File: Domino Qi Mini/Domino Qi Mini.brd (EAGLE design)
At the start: 55.9 x 33 mm, 97 parts, among them J1 MH22-1, J2 MH22-1, M1 DOMINO, Q1 AP2302GN, Q2 2SC4081, SW1 IT-1100, SW2 IT-1100, SW3 IT-1100, U1 ATMEGA32U4-XUMU, U2 MP2162GQH, U3 NTB0104GU12, U4 NTB0102GU, U5 MAX3375EEKA+T, Y1 16MHz

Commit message: Domino Qi Mini: work in progress
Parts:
- removed U$39: (no value), Domino:RECYCLE_BIN_LOGO
- removed U$41: (no value), Domino:CE_LOGO_SMALL
- removed U$9: (no value), Domino:DOMINO_LOGO_SMALL
- added U$3, U$5: (no value), Domino:DOMINO_QI_LOGO_SMALL
- S1: value USB_MR5-003A -> USB_MR5-001; device Domino:USB_MR5-003A -> Domino:USB-MR5-001
- SW1, SW2, SW3: value IT-1100 -> IT-1210; device Domino:IT-1100 -> Domino:IT-1210
- U$7: value (none) -> DOMINO_QI_LOGO; device Domino:DOMINO_LOGO_SMALL -> Domino:DOMINO_QI_LOGO
- U1: value ATMEGA32U4-XUMU -> ATMEGA32U4-XUAU/MU; device Domino:QFN44ML7X7 -> Domino:ATMEGA32U4_DUAL_FOOTPRINT
- moved U$7 98.7 mm to (-34.3, -47.0)
- moved SW2 60.9 mm to (0.64, 6.48), flipped to the bottom, turned to 270 degrees
- moved SW3 56.7 mm to (54.9, 26.9)
- moved SW1 46.3 mm to (0.64, 26.4), flipped to the bottom, turned to 270 degrees
- moved R23 45.2 mm to (51.8, 24.8), turned to 270 degrees
- moved C29 43.8 mm to (50.8, 24.8), turned to 90 degrees
- moved D9 37.9 mm to (41.6, 4.39), flipped to the bottom
- moved C14 34.2 mm to (31.9, 7.49), flipped to the bottom, turned to 270 degrees
- moved U1 34.1 mm to (27.9, 15.2), flipped to the bottom, turned to 180 degrees
- moved D8 33.8 mm to (22.5, 28.5), flipped to the bottom
- moved R8 33.5 mm to (20.4, 6.48), flipped to the bottom
- moved U4 32.2 mm to (22.7, 7.24), flipped to the bottom
- moved R17 31.6 mm to (25.0, 5.97), flipped to the bottom
- moved Q1 30.8 mm to (11.4, 27.9), flipped to the bottom
- moved C27 30.7 mm to (24.5, 7.49), flipped to the bottom, turned to 90 degrees
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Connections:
- net !RESET: now also SW1.1, U1.13A, U1.13M; no longer SW1.2, U1.13
- net +5V: now also U1.14A, U1.14M, U1.24A, U1.24M, U1.2A, U1.2M, U1.34A, U1.34M, U1.44A, U1.44M, U1.7A, U1.7M; no longer U1.14, U1.2, U1.24, U1.34, U1.44, U1.7
- net A0: now also U1.36A, U1.36M; no longer U1.36
- net A1: now also U1.37A, U1.37M; no longer U1.37
- net A2: now also U1.38A, U1.38M; no longer U1.38
- net A3: now also U1.39A, U1.39M; no longer U1.39
- net A4: now also U1.40A, U1.40M; no longer U1.40
- net A5: now also U1.41A, U1.41M; no longer U1.41
- net AREF: now also U1.42A, U1.42M; no longer U1.42
- net D+: now also D1.2; no longer D1.3
- net D-: now also D1.3; no longer D1.2
- net D4: now also U1.25A, U1.25M; no longer U1.25
- net D5: now also U1.31A, U1.31M; no longer U1.31
- net D6: now also U1.27A, U1.27M; no longer U1.27
- net GND: now also SW1.2, SW1.SH$1, SW1.SH$2, SW2.SH$1, SW2.SH$2, SW3.SH$1, SW3.SH$2, U1.15A, U1.15M, U1.23A, U1.23M, U1.35A, U1.35M, U1.43A, U1.43M, U1.5A, U1.5M, U1.PAD; no longer SW1.1, SW1.S$1, SW1.S$2, SW2.S$1, SW2.S$2, SW3.S$1, SW3.S$2, U1.15, U1.23, U1.35, U1.43, U1.5, U1.EXP
- net HANDSHAKE: now also U1.1A, U1.1M; no longer U1.1
- net IO10: now also U1.30A, U1.30M; no longer U1.30
- net IO11: now also U1.12A, U1.12M; no longer U1.12
- net IO12: now also U1.26M
- net IO13: now also U1.32A, U1.32M; no longer U1.32
- net IO8: now also U1.28A, U1.28M; no longer U1.28
- net IO9: now also U1.29A, U1.29M; no longer U1.29
- net MISO: now also U1.11A, U1.11M; no longer U1.11
- net MOSI: now also U1.10A, U1.10M; no longer U1.10
- net N$5: now also U1.3A, U1.3M; no longer U1.3
- net N$8: now also U1.33A, U1.33M; no longer U1.33
- net N$9: now also U1.4A, U1.4M; no longer U1.4
- net PE: now also S1.SH$1, S1.SH$2, S1.SH$3, S1.SH$4; no longer S1.S$1, S1.S$2, S1.S$3
- net RXD1: now also U1.20A, U1.20M; no longer U1.20
- net SCK: now also U1.9A, U1.9M; no longer U1.9
- net SCL: now also U1.18A, U1.18M; no longer U1.18
- net SDA: now also U1.19A, U1.19M; no longer U1.19
- net SS: now also U1.8A, U1.8M; no longer U1.8
- net TXD1: now also U1.21A, U1.21M; no longer U1.21
- net UCAP: now also U1.6A, U1.6M; no longer U1.6
- net XTAL1: now also U1.17A, U1.17M; no longer U1.17
- net XTAL2: now also U1.16A, U1.16M; no longer U1.16
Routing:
- net UART_RTS: track 75.6 -> 0.00 mm, vias 3 -> 0
- net GP6: track 0.00 -> 53.6 mm, vias 0 -> 3
- net AREF: track 0.00 -> 51.0 mm, vias 0 -> 3
- net +5V: track 46.5 -> 96.3 mm, vias 1 -> 2
- net I2S_MCK: track 7.10 -> 47.1 mm, vias 1 -> 3
- net MISO: track 0.00 -> 38.5 mm, vias 0 -> 1
- net SPDIF_OUT: track 8.13 -> 46.5 mm
- net !RESET: track 0.00 -> 37.7 mm
- net SS: track 0.00 -> 36.6 mm, vias 0 -> 1
- net A0: track 0.00 -> 36.4 mm, vias 0 -> 1
- net D6: track 0.00 -> 35.5 mm, vias 0 -> 1
- net MOSI: track 0.00 -> 35.2 mm, vias 0 -> 1
- net SCK: track 0.00 -> 34.8 mm, vias 0 -> 1
- net A1: track 0.00 -> 34.0 mm, vias 0 -> 1
- net D5: track 0.00 -> 33.6 mm, vias 0 -> 1
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- removed copper zone on layer 16, net +2V5
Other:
- board text removed: "CTS"
- board text removed: "Domino Core"
- board text removed: "Domino Pi"
- board text removed: "Domino Qi"
- board text removed: "MCK"
- board text removed: "MICIN"
- board text removed: "RTS"
- board text removed: "RX"
- board text removed: "SD"
- board text removed: "TX"
- board text removed: "WS"

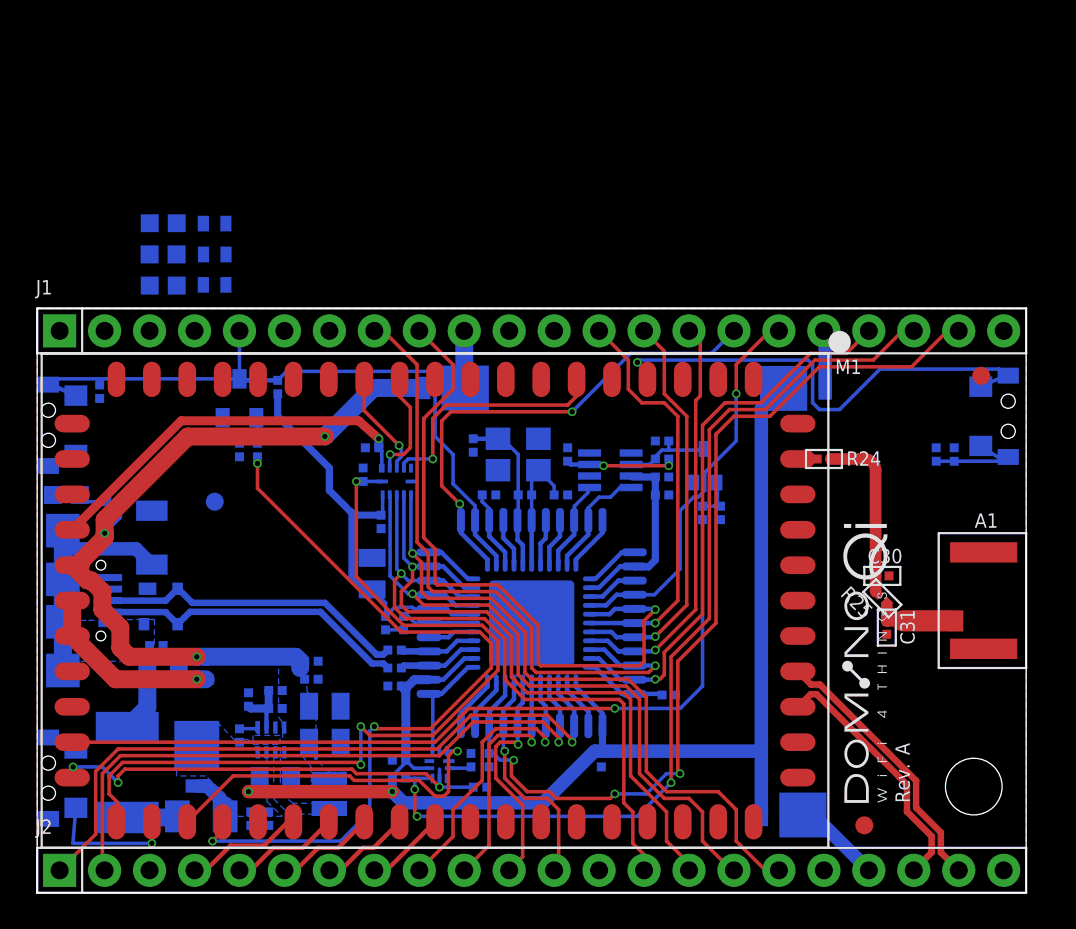
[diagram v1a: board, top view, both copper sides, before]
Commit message: Work in progress: changed for PCB antenna and removed Schottky diode on Domino Qi Mini, first Domino Qi draft
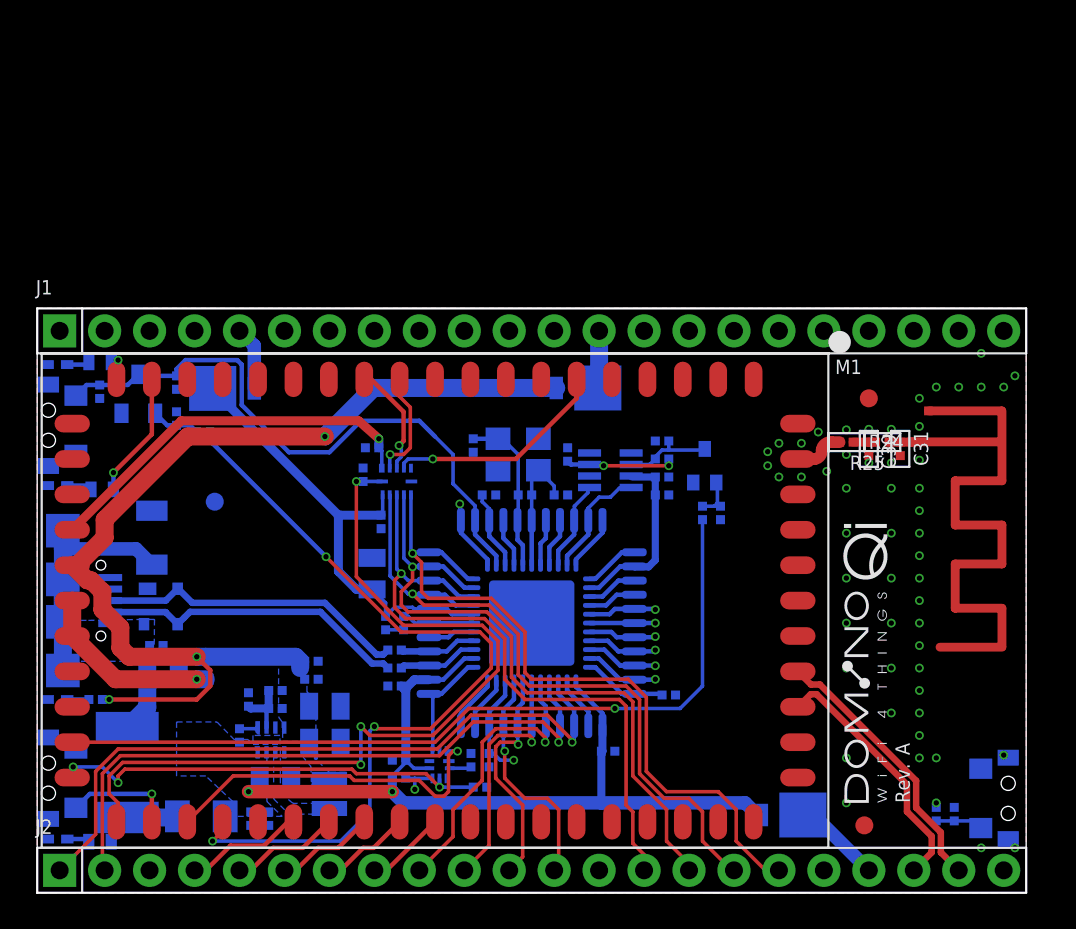
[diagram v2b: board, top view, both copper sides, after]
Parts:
- removed D2: MBRM130LT1G, Domino:DO-216AA
- A1: value ACA-5036-A2-CC-S -> RF_ANT1; device Domino:ACA-5036-A2-CC-S -> Domino:RF_ANT1
- D3, D4, D5, D6: device Domino:LED0603 -> Domino:LED0402
- moved R20 35.5 mm to (3.55, 2.89), turned to 180 degrees
- moved D4 35.3 mm to (1.15, 3.04)
- moved D7 32.3 mm to (11.6, 28.5)
- moved SW3 21.6 mm to (54.9, 5.33)
- moved C29 20.3 mm to (50.8, 4.45)
- moved R23 20.3 mm to (51.8, 4.45)
- moved R21 13.2 mm to (3.67, 22.8), turned to 180 degrees
- moved D5 12.8 mm to (1.15, 23.0)
- moved D3 11.6 mm to (1.14, 10.9)
- moved A1 11.3 mm to (49.9, 27.2)
- moved R18 11.2 mm to (3.30, 10.9)
- moved C31 10.1 mm to (48.8, 25.1)
- moved R22 8.89 mm to (3.56, 30.0)
- moved R25 8.83 mm to (47.8, 25.5), turned to 0 degrees
- moved D6 8.62 mm to (1.14, 29.8)
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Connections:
- removed net +VUSB: D2.2, L1.1
- net !RESET: now also J1.18; no longer J1.5
- net +5V: now also L1.1; no longer D2.1
- net 3V3: now also J1.13; no longer J1.10
- net AREF: now also J1.2; no longer J1.21
- net D4: now also J1.16; no longer J1.7
- net D5: now also J1.15; no longer J1.8
- net D6: now also J1.14; no longer J1.9
- net GND: now also A1.GND, J1.12; no longer A1.GND$1, A1.GND$2, J1.11
- net GP6: now also J1.3; no longer J1.20
- net HANDSHAKE: now also J1.11; no longer J1.12
- net IO10: now also J1.8; no longer J1.15
- net IO11: now also J1.7; no longer J1.16
- net IO12: now also J1.6; no longer J1.17
- net IO13: now also J1.4; no longer J1.19
- net IO8: now also J1.10; no longer J1.13
- net IO9: now also J1.9; no longer J1.14
- net RXD1: now also J1.21; no longer J1.2
- net SCL: now also J1.17; no longer J1.6
- net SDA: now also J1.19; no longer J1.4
- net TXD1: now also J1.20; no longer J1.3
- net VIN: now also J1.5; no longer J1.18
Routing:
- net GP6: track 53.6 -> 2.13 mm, vias 3 -> 1
- net AREF: track 51.0 -> 3.13 mm, vias 3 -> 1
- net D6: track 35.5 -> 1.20 mm
- net D5: track 33.6 -> 1.19 mm
- net IO13: track 28.4 -> 1.20 mm
- net !RESET_L: track 27.1 -> 0.39 mm, vias 1 -> 0
- net IO11: track 24.8 -> 1.08 mm, vias 2 -> 1
- net IO8: track 20.8 -> 1.18 mm
- net IO12: track 19.4 -> 0.00 mm, vias 1 -> 0
- net IO10: track 20.6 -> 1.22 mm
- net IO9: track 20.2 -> 1.20 mm
- net +5V: track 96.3 -> 78.4 mm
- net +3V3: track 44.7 -> 58.5 mm
- net ANT0_EXT: track 9.82 -> 1.27 mm
- net LED1: track 0.77 -> 7.88 mm, vias 0 -> 1
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
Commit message: Work in progress on Domino Qi Mini board
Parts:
- removed C2: 10u, Domino:C0805
- removed C3: 100n, Domino:C0402
- removed D7, D8, D9: MBRM130LT1G, Domino:DO-216AA
- removed F1: 0ZCG0110FF2C, Domino:PTC1812
- removed L1: BLM31PG601SN1L, Domino:FB1206
- added C32: 100n, Domino:C0402
- added C33: 4u7, Domino:C0805
- added C34: 10n, Domino:C0402
- added L3: BLM31PG601SN1L, Domino:FB1206
- added R26: 100k, Domino:R0402
- added R27: 15k, Domino:R0402
- added R28: 0R, Domino:R0402
- added U6: MP65151DJ, Domino:SOT23-6
- R1, R2: device GeMiNi:R0402 -> Domino:R0402
- moved U$42 7.05 mm to (15.7, 2.79), turned to 270 degrees
- moved C25 6.13 mm to (9.40, 12.4), turned to 90 degrees
- moved R18 5.99 mm to (9.02, 9.14)
- moved L2 5.47 mm to (16.3, 11.0)
- moved R14 5.22 mm to (5.97, 22.1)
- moved C24 5.09 mm to (10.4, 12.4), turned to 90 degrees
- moved C22 4.67 mm to (11.9, 12.3), turned to 90 degrees
- moved C23 4.44 mm to (14.0, 12.3), turned to 90 degrees
- moved R12 4.15 mm to (5.97, 23.1), turned to 180 degrees
- moved C16 3.07 mm to (11.0, 9.53), turned to 90 degrees
- moved R6 2.95 mm to (11.6, 8.00), turned to 180 degrees
- moved Q1 2.85 mm to (4.70, 25.5)
- moved R5 2.57 mm to (13.6, 7.49), turned to 0 degrees
- moved R9 2.40 mm to (5.84, 27.6)
- moved R8 2.16 mm to (22.0, 4.95), turned to 270 degrees
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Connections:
- removed net 5V: D9.1, J2.19
- removed net VPROT: F1.1, L1.2
- new net !FLAG: R28.1, U6.4
- new net EN_USB: R26.1, R28.2, U6.3
- new net ILIM: R27.1, U6.5
- net +3V3: now also J1.13; no longer D8.2
- net +5V: now also J1.5, J2.19, U6.6; no longer D7.1, D9.2, L1.1
- net 3V3: no longer D8.1, J1.13
- net GND: now also C32.2, C33.2, C34.2, R27.2, U6.2; no longer C2.2, C3.2
- net VBUS: now also C34.1, L3.2; no longer C2.1, C3.1, F1.2
- net VIN: now also C32.1, C33.1, L3.1, R26.2, U6.1; no longer D7.2, J1.5
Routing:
- net !RESET_L: track 0.39 -> 33.4 mm, vias 0 -> 1
- net D5: track 1.19 -> 26.4 mm, vias 1 -> 3
- net UART_RTS: track 0.00 -> 25.0 mm, vias 0 -> 1
- net RXD1: track 2.22 -> 26.8 mm, vias 0 -> 1
- net SDA: track 0.00 -> 22.7 mm, vias 0 -> 1
- net +3V3: track 58.5 -> 37.2 mm, vias 3 -> 4
- net TXD1: track 3.62 -> 24.8 mm, vias 0 -> 1
- net LED6: track 0.00 -> 20.3 mm, vias 0 -> 2
- net SCL: track 0.00 -> 20.0 mm, vias 0 -> 1
- net D4: track 0.00 -> 17.0 mm, vias 0 -> 1
- net !RESET: track 31.7 -> 42.6 mm, vias 0 -> 2
- net POWER_LED: track 1.23 -> 7.59 mm
- net +3.3VD_IN: track 10.9 -> 15.9 mm, vias 1 -> 3
- net 5V: track 5.02 -> 0.00 mm
- net +5V: track 78.4 -> 73.6 mm, vias 2 -> 0
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- added copper zone on layer 16, net VIN
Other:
- board text added: "c 2014-2015, Domino Team All rights reserved."
- board text added: "© 2014-2015, The Domino Team. All rights reserved."
- board text removed: "SLOT SIZE IN MM 2x PLATED SLOT: 0.9x0.4"
- board text removed: "SLOT SIZE IN MM 2x PLATED SLOT: 1.3x0.5"
- board text removed: "c 2014, Domino Team All rights reserved."
- board text removed: "© 2014, The Domino Team. All rights reserved."

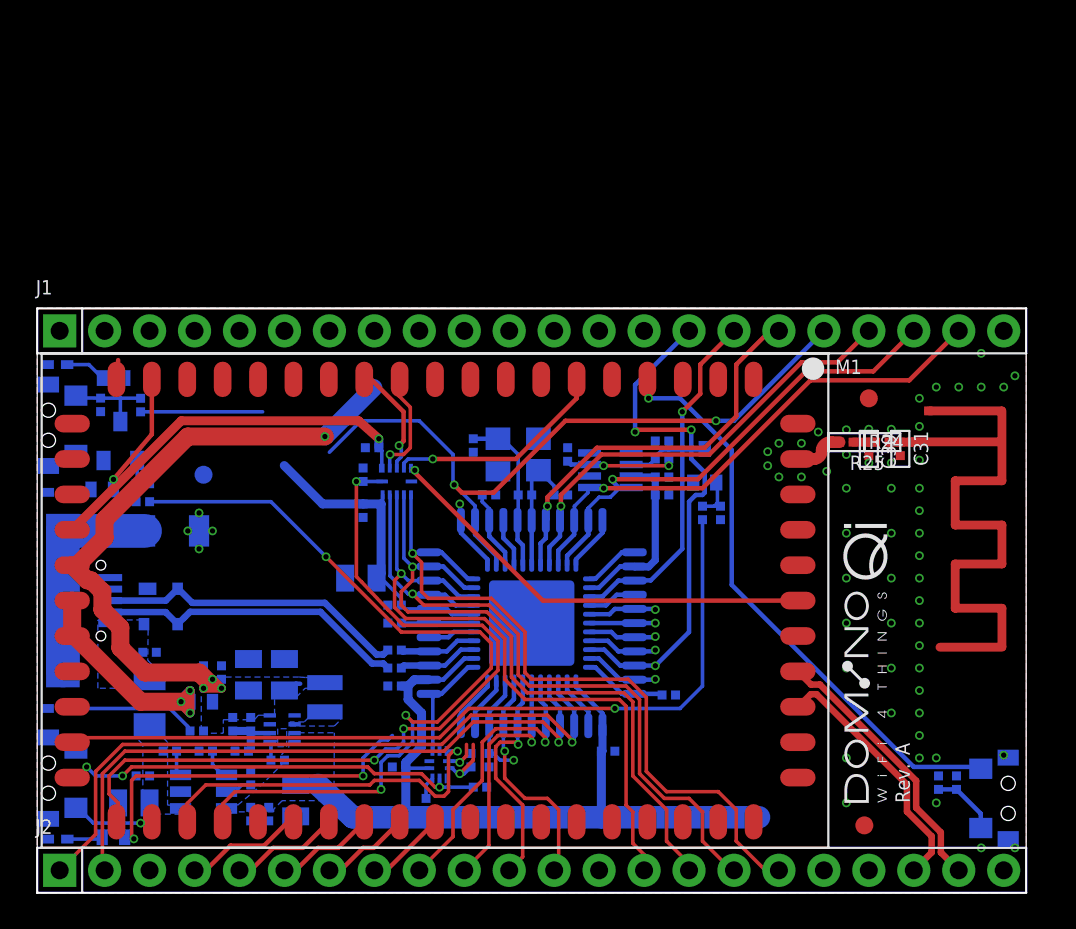
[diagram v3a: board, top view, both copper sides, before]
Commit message: Work in progress on Domino Qi Mini board: clustered all voltage translator chips instead of putting them close to ATMega32U4
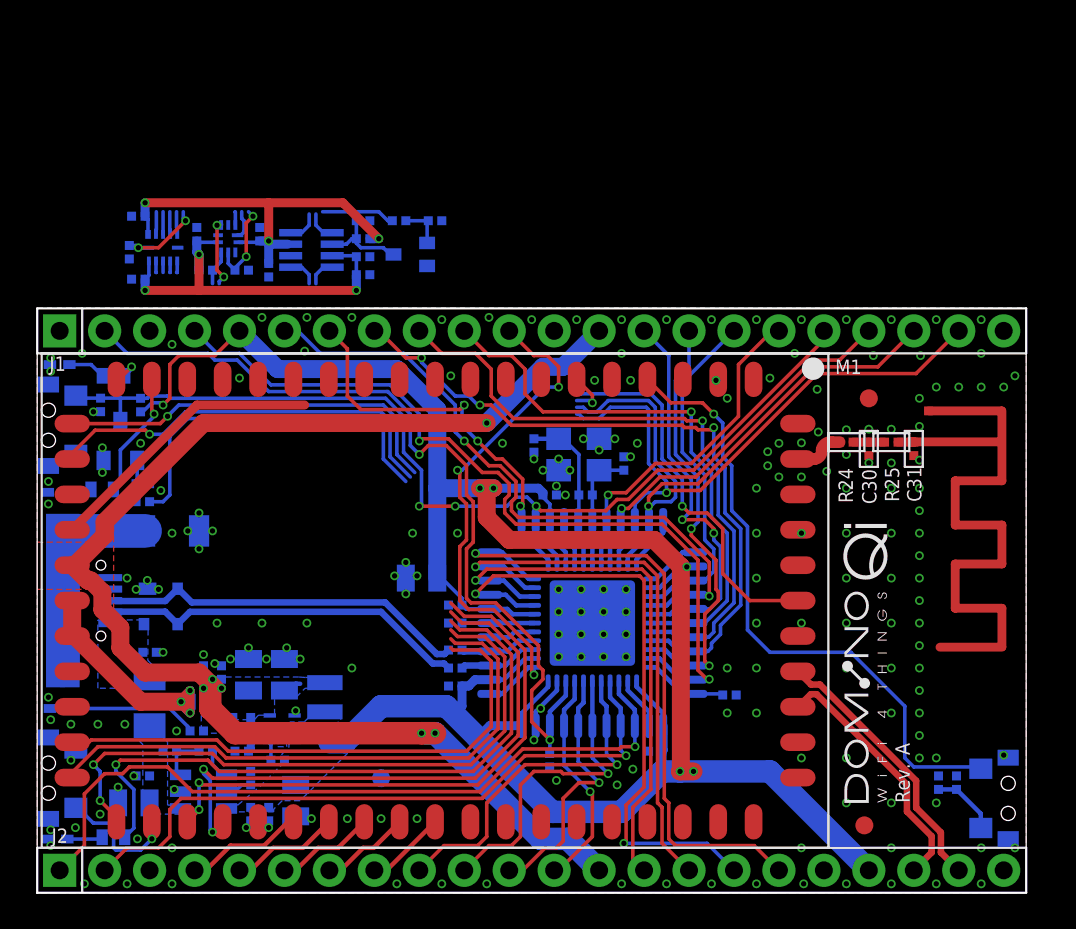
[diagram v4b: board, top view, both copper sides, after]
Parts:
- added DRILEGEND: (no value), drilegend:DRILEGEND
- moved R8 32.7 mm to (9.53, 35.2), turned to 0 degrees
- moved C20 32.2 mm to (9.02, 37.2), turned to 90 degrees
- moved R17 32.2 mm to (11.6, 35.2)
- moved U4 32.0 mm to (10.8, 37.0)
- moved C27 32.0 mm to (12.6, 37.2)
- moved R15 23.8 mm to (20.4, 38.0), turned to 0 degrees
- moved R13 23.1 mm to (22.5, 38.0), turned to 180 degrees
- moved C18 21.0 mm to (18.4, 35.9)
- moved R10 21.0 mm to (18.4, 37.0)
- moved U5 21.0 mm to (15.5, 36.3)
- moved C21 21.0 mm to (18.4, 34.9)
- moved R11 21.0 mm to (18.4, 38.0), turned to 180 degrees
- moved Q2 20.5 mm to (21.1, 36.1), turned to 270 degrees
- moved F2 19.9 mm to (19.4, 6.48)
- moved C28 19.8 mm to (13.1, 35.2), turned to 270 degrees
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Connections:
- removed net 3V3: J2.13
- net +3V3: now also J2.13
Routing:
- net +5V: track 73.6 -> 138.9 mm, vias 0 -> 9
- net IO13: track 1.20 -> 44.0 mm, vias 1 -> 2
- net AREF: track 3.13 -> 45.7 mm, vias 1 -> 2
- net +3V3: track 37.2 -> 78.8 mm, vias 4 -> 6
- net IO10: track 1.22 -> 36.5 mm, vias 1 -> 3
- net IO12: track 0.00 -> 34.4 mm, vias 0 -> 2
- net IO9: track 1.20 -> 33.3 mm
- net IO8: track 1.18 -> 29.4 mm
- net HANDSHAKE: track 3.32 -> 31.2 mm, vias 0 -> 5
- net UART_TX: track 0.00 -> 25.2 mm, vias 0 -> 1
- net UART_RX: track 0.00 -> 24.3 mm, vias 0 -> 1
- net IO11: track 1.08 -> 19.8 mm, vias 1 -> 3
- net D6: track 1.20 -> 19.8 mm, vias 1 -> 2
- net LED6: track 20.3 -> 37.0 mm, vias 2 -> 1
- net I2S_MICIN: track 24.4 -> 38.0 mm, vias 3 -> 2
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- added copper zone on layer 1, net +3V3
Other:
- board text added: "01-16"
- board text added: "01-20"
- board text added: "10~"
- board text added: "11~"
- board text added: "12"
- board text added: "13"
- board text added: "2"
- board text added: "2V"
- board text added: "3.3V"
- board text added: "3~"
- board text added: "4"
- board text added: "5V"
- board text added: "5~"
- board text added: "6~"
- board text added: "7"
- board text added: "8"
- board text added: "9~"
- board text added: "A0"
- board text added: "A1"
- board text added: "A2"
- board text added: "A3"
- board text added: "A4"
- board text added: "A5"
- board text added: "ANALOG IN"
- board text added: "AREF"
- board text added: "DIGITAL (PWM~)"
- board text added: "GP6"
- board text added: "ICSP"
- board text added: "LAYER-STACK"
- board text added: "RESET"
- board text added: "RX <- 0"
- board text added: "SCK"
- board text added: "SS"
- board text added: "TX -> 1"
- board text removed: "+2V5"
- board text removed: "+3v3"
- board text removed: "ETH0"
- board text removed: "ETH4"
- board text removed: "ETH_P0"
- board text removed: "I2S"
- board text removed: "I2S_CK"
- board text removed: "I2S_MCK"
- board text removed: "I2S_MICIN"
- board text removed: "I2S_SD"
- board text removed: "I2S_WS"
- board text removed: "JTAG_TCK"
- board text removed: "JTAG_TDI"
- board text removed: "JTAG_TDO"
- board text removed: "JTAG_TMS"
- board text removed: "LED"
- board text removed: "P0_RX+"
- board text removed: "P0_RX-"
- board text removed: "P0_TX+"
- board text removed: "P0_TX-"
- board text removed: "SPDIF_OUT"
- board text removed: "SPI_CLK"
- board text removed: "SPI_CS"
- board text removed: "SPI_MISO"
- board text removed: "SPI_MOSI"
- board text removed: "UART"
- board text removed: "UART_CTS"
- board text removed: "UART_RTS"
- board text removed: "UART_RX"
- board text removed: "UART_TX"
